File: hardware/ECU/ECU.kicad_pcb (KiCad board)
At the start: 4 copper layers, 58 x 69 mm, 75 parts, among them IC1 IR4427SPBF, IC2 EL357NB_TA_-G, IC3 EL357NB_TA_-G, J1 USB_B_Micro, J2 TFP09-2-12B, J3 Connector, Q1 S8050, Q2 S8050, Q3 RJP63K2, Q4 RJP63K2, SW1 RESET, SW2 EN, U1 AMS1117-3.3, U2 AMS1117-3.3, U3 CP2102N-Axx-xQFN28, U4 ESP32-WROOM-32U

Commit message: ECU hardware v0.2 candidate
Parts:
- removed C15: 22u, Capacitor_SMD:C_0603_1608Metric_Pad1.08x0.95mm_HandSolder
- removed C22, C23: 1n, Capacitor_SMD:C_0603_1608Metric_Pad1.08x0.95mm_HandSolder
- removed D11: LED, LED_SMD:LED_0603_1608Metric_Pad1.05x0.95mm_HandSolder
- removed Q2: S8050, Package_TO_SOT_SMD:SOT-23
- removed U3: CP2102N-Axx-xQFN28, Package_DFN_QFN:QFN-28-1EP_5x5mm_P0.5mm_EP3.35x3.35mm
- added C24: 100n, Capacitor_SMD:C_0603_1608Metric, F.Cu at (154.6, 133.4)
- added C25: 100n, Capacitor_SMD:C_0603_1608Metric, F.Cu at (149.2, 130.9)
- added C26: 100n, Capacitor_SMD:C_0603_1608Metric, F.Cu at (150.0, 114.3)
- added C27: 100n, Capacitor_SMD:C_0603_1608Metric, F.Cu at (146.1, 79.4)
- added C28: 100n, Capacitor_SMD:C_0603_1608Metric, F.Cu at (150.6, 79.4)
- added C29: 100n, Capacitor_SMD:C_0603_1608Metric, F.Cu at (152.9, 83.0)
- added IC4: ESP32-S3-WROOM-1U-N8R8, MyLibrary:ESP32S3WROOM1UN4, F.Cu at (130.1, 111.0)
- added IC5: EL357NB_TA_-G, MyLibrary:EL357NG, F.Cu at (150.8, 109.3)
- added J4: USB_B, Connector_USB:USB_B_TE_5787834_Vertical, F.Cu at (128.4, 87.9)
- added J5: BATTERY, Connector_Molex:Molex_KK-396_5273-02A_1x02_P3.96mm_Vertical, F.Cu at (165.4, 124.2)
- added J6: GATEs, Connector_Molex:Molex_KK-396_5273-06A_1x06_P3.96mm_Vertical, F.Cu at (209.7, 83.3)
- added J8: CAPTURE_TRG, Connector_JST:JST_XH_B2B-XH-A_1x02_P2.50mm_Vertical, F.Cu at (149.2, 118.2)
- added JP1: BOOT, Connector_PinHeader_2.54mm:PinHeader_1x02_P2.54mm_Vertical, F.Cu at (117.0, 118.0)
- added L1: 100u, MyLibrary:INDPM102100X400N, F.Cu at (187.2, 121.3)
- added R26: 10k, Resistor_SMD:R_0603_1608Metric_Pad0.98x0.95mm_HandSolder, F.Cu at (146.1, 86.3)
- added R27: 100, Resistor_SMD:R_0603_1608Metric_Pad0.98x0.95mm_HandSolder, F.Cu at (135.0, 95.9)
- added R28: 100, Resistor_SMD:R_0603_1608Metric_Pad0.98x0.95mm_HandSolder, F.Cu at (136.9, 85.0)
- added R30: 1k, Resistor_SMD:R_0603_1608Metric_Pad0.98x0.95mm_HandSolder, F.Cu at (134.1, 84.1)
- added R31: 1k, Resistor_SMD:R_0603_1608Metric_Pad0.98x0.95mm_HandSolder, F.Cu at (142.5, 121.2)
- added R32: 10k, Resistor_SMD:R_0603_1608Metric_Pad0.98x0.95mm_HandSolder, F.Cu at (149.1, 86.3)
- added R33: 100, Resistor_SMD:R_0603_1608Metric_Pad0.98x0.95mm_HandSolder, F.Cu at (143.8, 79.8)
- added R34: 100, Resistor_SMD:R_0603_1608Metric_Pad0.98x0.95mm_HandSolder, F.Cu at (152.9, 79.8)
- added R35: 10k, Resistor_SMD:R_0603_1608Metric_Pad0.98x0.95mm_HandSolder, F.Cu at (150.6, 86.3)
- added R36: 100, Resistor_SMD:R_0603_1608Metric_Pad0.98x0.95mm_HandSolder, F.Cu at (149.1, 78.6)
- added R37: 100, Resistor_SMD:R_0603_1608Metric_Pad0.98x0.95mm_HandSolder, F.Cu at (147.6, 78.6)
- added R38: 0, Resistor_SMD:R_0603_1608Metric_Pad0.98x0.95mm_HandSolder, F.Cu at (176.9, 106.8)
- added R39: 100, Resistor_SMD:R_0603_1608Metric_Pad0.98x0.95mm_HandSolder, F.Cu at (156.3, 133.5)
- added R42: 10k, Resistor_SMD:R_0603_1608Metric_Pad0.98x0.95mm_HandSolder, F.Cu at (152.6, 136.3)
- added R43: 10k, Resistor_SMD:R_0603_1608Metric_Pad0.98x0.95mm_HandSolder, F.Cu at (149.1, 136.3)
- added R45: 0.01, MyLibrary:RESC10052X106N, F.Cu at (165.4, 133.6)
- added R47: 130k, Resistor_SMD:R_0603_1608Metric_Pad0.98x0.95mm_HandSolder, F.Cu at (152.4, 129.4)
- added R50: 5.6k, Resistor_SMD:R_0603_1608Metric_Pad0.98x0.95mm_HandSolder, F.Cu at (152.4, 130.9)
- added R51: 10k, Resistor_SMD:R_0603_1608Metric_Pad0.98x0.95mm_HandSolder, F.Cu at (144.7, 133.7)
- added R52: 1k, Resistor_SMD:R_0603_1608Metric_Pad0.98x0.95mm_HandSolder, F.Cu at (146.7, 114.3)
- added R53: 1k, Resistor_SMD:R_0603_1608Metric_Pad0.98x0.95mm_HandSolder, F.Cu at (141.5, 113.7)
- added R54: 1k, Resistor_SMD:R_0603_1608Metric_Pad0.98x0.95mm_HandSolder, F.Cu at (137.5, 71.8)
- added U5: ADS1115IDGS, Package_SO:TSSOP-10_3x3mm_P0.5mm, F.Cu at (149.5, 133.6)
- added U6: INA180A3, Package_TO_SOT_SMD:SOT-23-5, F.Cu at (159.5, 133.6)
- added U7: SRV05-4, Package_TO_SOT_SMD:SOT-23-6, F.Cu at (122.6, 97.5)
- C10, C12: value 10u -> 100n; footprint Capacitor_SMD:C_0603_1608Metric_Pad1.08x0.95mm_HandSolder -> Capacitor_SMD:C_0603_1608Metric
- C11: footprint Capacitor_SMD:C_0603_1608Metric_Pad1.08x0.95mm_HandSolder -> Capacitor_SMD:C_0603_1608Metric
- C13: value 1n -> 100n; footprint Capacitor_SMD:C_0603_1608Metric_Pad1.08x0.95mm_HandSolder -> Capacitor_SMD:C_0603_1608Metric
- C14: footprint Capacitor_SMD:C_0603_1608Metric_Pad1.08x0.95mm_HandSolder -> Capacitor_SMD:C_0603_1608Metric; moved to F.Cu
- C16, D1, R2: moved to F.Cu
- C21: value 1n -> 100n; footprint Capacitor_SMD:C_0603_1608Metric_Pad1.08x0.95mm_HandSolder -> Capacitor_SMD:C_0603_1608Metric; moved to B.Cu
- C3, C4: footprint Capacitor_SMD:C_0805_2012Metric_Pad1.18x1.45mm_HandSolder -> Capacitor_SMD:C_0603_1608Metric
- C5: value 100n -> 1u; footprint Capacitor_SMD:C_0805_2012Metric_Pad1.18x1.45mm_HandSolder -> Capacitor_SMD:C_0603_1608Metric
- C8: value 22u -> 100u; footprint Capacitor_SMD:C_0805_2012Metric_Pad1.18x1.45mm_HandSolder -> Capacitor_SMD:CP_Elec_10x10
- C9: value 100n -> 1n; footprint Capacitor_SMD:C_0603_1608Metric_Pad1.08x0.95mm_HandSolder -> Capacitor_SMD:CP_Elec_10x10
- D10: value 1n4007 -> m7
- D3: value LED -> ss36; footprint LED_SMD:LED_0603_1608Metric_Pad1.05x0.95mm_HandSolder -> Diode_SMD:D_SMC; moved to F.Cu
- D4: value 3.6v -> 5v
- D5: value 1n4001 -> LED; footprint Diode_SMD:D_SMA -> LED_SMD:LED_0603_1608Metric_Pad1.05x0.95mm_HandSolder
- D6: value 5v -> ss36; footprint Diode_SMD:D_SOD-523 -> Diode_SMD:D_SMC
- D7: value 5v -> m7; footprint Diode_SMD:D_SOD-523 -> Diode_SMD:D_SMA
- D8: value LED -> ss36; footprint LED_SMD:LED_0603_1608Metric_Pad1.05x0.95mm_HandSolder -> Diode_SMD:D_SMC
- IC1: footprint My_Lirbrary:SOIC127P600X175-8N -> MyLibrary:SOIC127P600X175-8N
- IC2, IC3: footprint My_Lirbrary:SOP254P700X200-4N -> MyLibrary:EL357NG
- J1: value USB_B_Micro -> AQS; footprint Connector_USB:USB_Micro-B_Molex-105017-0001 -> Connector_JST:JST_XH_B6B-XH-A_1x06_P2.50mm_Vertical
- J2: footprint My_Lirbrary:TFP09212B -> MyLibrary:TFP09212B
- J3: value Connector -> CAM_SENSOR; footprint Connector_PinHeader_2.54mm:PinHeader_2x06_P2.54mm_Vertical -> Connector_JST:JST_XH_B6B-XH-A_1x06_P2.50mm_Vertical
- Q1: value S8050 -> RJP63K2; footprint Package_TO_SOT_SMD:SOT-23 -> Package_TO_SOT_SMD:TO-263-2; moved to F.Cu
- R1: value 1M -> 10k; moved to F.Cu
- R16, R17, R18, R19, R20, R21: footprint Resistor_SMD:R_0603_1608Metric_Pad0.98x0.95mm_HandSolder -> Resistor_SMD:R_0603_1608Metric; moved to F.Cu
- R22, R23: value 470 -> 10k
- R24: value 5k -> 10k
- R25: value 1k -> 10k
- R3: value 2k -> 10k; moved to F.Cu
- R4, R5, R8: value 12k -> 10k; moved to F.Cu
- R6, R7: value 0 -> 10k
- R9: value 2k -> 100
- SW1: value RESET -> RESET BTN; footprint Button_Switch_SMD:SW_Push_1P1T_NO_CK_KMR2 -> Button_Switch_SMD:SW_SPST_PTS810
- SW2: value EN -> ZERO BTN; footprint Button_Switch_SMD:SW_Push_1P1T_NO_CK_KMR2 -> Button_Switch_SMD:SW_SPST_PTS810
- U1: value AMS1117-3.3 -> LM2576S-5; footprint Package_TO_SOT_SMD:SOT-223-3_TabPin2 -> Package_TO_SOT_SMD:TO-263-5_TabPin3
- U4: value ESP32-WROOM-32U -> ADS1115IDGS; footprint RF_Module:ESP32-WROOM-32U -> Package_SO:TSSOP-10_3x3mm_P0.5mm
- moved D10 81.3 mm to (159.7, 143.2), turned to 0 degrees
- moved C8 77.2 mm to (209.8, 134.6), turned to -90 degrees
- moved C2 70.4 mm to (118.0, 141.2), turned to 180 degrees
- moved C7 70.4 mm to (118.0, 139.1), turned to 180 degrees
- moved D3 67.6 mm to (201.3, 124.2), turned to 0 degrees
- moved C6 67.4 mm to (119.0, 127.3)
- moved C1 67.4 mm to (119.0, 125.2)
- moved U2 66.1 mm to (118.0, 133.1), turned to 90 degrees
- moved U1 64.3 mm to (196.2, 138.3)
- moved R22 62.5 mm to (119.8, 98.6), turned to 90 degrees
- moved R5 61.0 mm to (143.8, 136.1), turned to 90 degrees
- moved R24 60.8 mm to (144.7, 132.1), turned to 180 degrees
- moved R4 59.5 mm to (145.3, 137.0), turned to 90 degrees
- moved R8 59.0 mm to (113.2, 111.9)
- moved Q4 57.6 mm to (188.6, 93.2), turned to 0 degrees
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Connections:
- net Net-(J2-CD/DAT3) renamed /SD_DAT3
- net Net-(J2-DAT2) renamed /SD_DAT2
- C10 pad 1: VBUS -> GND
- C10 pad 2: GND -> +3.3V
- C11 pad 1: +3.3V -> GND
- C11 pad 2: GND -> Net-(C11-Pad2)
- C12 pad 1: +3.3V -> GND
- C12 pad 2: GND -> Net-(C12-Pad2)
- C13 pad 1: /EN -> GND
- C13 pad 2: GND -> +3.3V
- C14 pad 2: +3.3V -> Net-(U4-AIN3)
- C18 pad 1: +12V -> +BATT
- C19 pad 1: +12V -> +BATT
- C2 pad 1: +12V -> +4V
- C21 pad 2: /O2 -> +3.3V
- C3 pad 1: VBUS -> GND
- C3 pad 2: GND -> +3.3V
- C4 pad 1: VBUS -> GND
- C4 pad 2: GND -> +3.3V
- C5 pad 1: +3.3V -> GND
- C5 pad 2: GND -> /RESET_PIN
- C7 pad 1: +12V -> +4V
- C8 pad 1: +3.3V -> +BATT
- C9 pad 1: VBUS -> +5V
- D10 pad 1: +12V -> +4V
- D10 pad 2: +BATT -> +5V
- D3 pad 1: GND -> Net-(D3-K)
- D3 pad 2: Net-(D3-A) -> GND
- D4 pad 1: +3.3V -> +4V
- D5 pad 1: VBUS -> Net-(D5-K)
- D5 pad 2: Net-(D5-A) -> /LED_PIN
- D6 pad 1: Net-(D6-K) -> +BATT
- D6 pad 2: GND -> /FUEL
- D7 pad 1: Net-(D7-K) -> +4V
- D7 pad 2: GND -> Net-(D7-A)
- D8 pad 1: GND -> +BATT
- D8 pad 2: Net-(D8-A) -> /PUMP
- IC1 pad 5: /COIL_IGBT -> Net-(IC1-OUT_B)
- IC1 pad 6: +12V -> +BATT
- IC1 pad 7: /FUEL_IGBT -> Net-(IC1-OUT_A)
- IC2 pad 1: /FUEL_PIN -> /COIL_PIN
- IC2 pad 4: +12V -> +BATT
- IC3 pad 1: /COIL_PIN -> /FUEL_PIN
- IC3 pad 4: +12V -> +BATT
- J1 pad 1: Net-(D5-A) -> GND
- J1 pad 2: Net-(D6-K) -> /IAT
- J1 pad 3: Net-(D7-K) -> /MPS
- J1 pad 4: unconnected-(J1-ID-Pad4) -> /TPS
- J1 pad 5: GND -> /AFR
- J1 pad 6: Net-(J1-Shield) -> +5V
- J2 pad 8: Net-(J2-DAT1) -> /SD_DAT1
- J3 pad 1: +BATT -> GND
- J3 pad 2: /FUEL -> /FSPI_CS
- J3 pad 3: GND -> /FSPI_MOSI
- J3 pad 4: /COIL -> /FSPI_CLK
- J3 pad 5: GND -> /FSPI_MISO
- J3 pad 6: GND -> +5V
- Q1 pad 1: Net-(Q1-E) -> Net-(Q1-G)
- Q1 pad 2: Net-(Q1-B) -> /PUMP
- Q1 pad 3: /EN -> GND
- R1 pad 1: Net-(J1-Shield) -> GND
- R1 pad 2: GND -> Net-(IC1-INA)
- R11 pad 2: /COIL_IGBT -> Net-(IC1-OUT_A)
- R15 pad 2: /FUEL_IGBT -> Net-(IC1-OUT_B)
- R2 pad 1: +12V -> +4V
- R21 pad 1: Net-(J2-DAT1) -> +3.3V
- R21 pad 2: +3.3V -> /SD_DAT1
- R22 pad 1: Net-(C22-Pad1) -> Net-(IC4-IO46)
- R22 pad 2: /IO0 -> GND
- R23 pad 1: Net-(C23-Pad1) -> GND
- R23 pad 2: /EN -> Net-(IC5-E)
- R24 pad 1: /IO0 -> Net-(U5-AIN2)
- R25 pad 1: GND -> /SDA_0
- R25 pad 2: Net-(D11-K) -> +3.3V
- R3 pad 1: VBUS -> GND
- R3 pad 2: Net-(D3-A) -> Net-(IC1-INB)
- R4 pad 1: Net-(Q2-E) -> +3.3V
- R4 pad 2: Net-(Q1-B) -> /SCL_1
- R5 pad 1: Net-(Q1-E) -> +3.3V
- R5 pad 2: Net-(Q2-B) -> /SDA_1
- R6 pad 1: Net-(U3-RXD) -> /RESET_PIN
- R6 pad 2: /RXD -> +3.3V
- R7 pad 2: /TXD -> +3.3V
- R8 pad 1: /EN -> GND
- R8 pad 2: +3.3V -> Net-(IC4-IO45)
- R9 pad 1: +3.3V -> GND
- R9 pad 2: Net-(D8-A) -> Net-(IC5-K)
- SW1 pad 2: Net-(C22-Pad1) -> Net-(C11-Pad2)
- SW2 pad 2: Net-(C23-Pad1) -> Net-(C12-Pad2)
- U1 pad 1: GND -> +BATT
- U1 pad 2: +3.3V -> Net-(D3-K)
- U1 pad 3: VBUS -> GND
- U2 pad 3: +12V -> +4V
- U4 pad 1: GND -> Net-(U4-ADDR)
- U4 pad 10: unconnected-(U4-IO25-Pad10) -> /SCL_0
- U4 pad 2: +3.3V -> Net-(U4-ALERT/RDY)
- U4 pad 3: /EN -> GND
- U4 pad 4: unconnected-(U4-SENSOR_VP-Pad4) -> Net-(U4-AIN0)
- U4 pad 5: unconnected-(U4-SENSOR_VN-Pad5) -> Net-(U4-AIN1)
- U4 pad 7: unconnected-(U4-IO35-Pad7) -> Net-(U4-AIN3)
- U4 pad 8: unconnected-(U4-IO32-Pad8) -> +3.3V
- U4 pad 9: unconnected-(U4-IO33-Pad9) -> /SDA_0
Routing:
- net +BATT: track 4.48 -> 257.3 mm, vias 0 -> 8
- net +5V: track 0.00 -> 195.7 mm, vias 0 -> 3
- net GND: track 3.96 -> 105.0 mm, vias 157 -> 195
- net +4V: track 0.00 -> 72.6 mm
- net Net-(D7-A): track 0.00 -> 48.3 mm, vias 0 -> 4
- net /FSPI_MISO: track 0.00 -> 46.3 mm
- net /FSPI_CLK: track 0.00 -> 44.2 mm
- net /FSPI_MOSI: track 0.00 -> 42.2 mm
- net /FSPI_CS: track 0.00 -> 40.1 mm
- net +12V: track 38.6 -> 0.00 mm, vias 6 -> 0
- net VBUS: track 38.3 -> 0.00 mm, vias 2 -> 0
- net /VSPI_MOSI: track 35.8 -> 0.00 mm, vias 1 -> 0
- net Net-(Q1-E): track 35.1 -> 0.00 mm, vias 1 -> 0
- net /SDA_0: track 0.00 -> 33.9 mm
- net /SCL_0: track 0.00 -> 32.2 mm
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- removed copper zone on In2.Cu, net +12V
- removed copper zone on In1.Cu, net GND
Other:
- board size 58 x 69 mm -> 115 x 100 mm
- copper layers 4 -> 2
- board text added: "+"
- board text added: "+5v"
- board text added: "-"
- board text added: "AFR"
- board text added: "BOOT"
- board text added: "CAMSHAFT SENSOR"
- board text added: "CPTR"
- board text added: "ECU v0.2 Author: Collyn"
- board text added: "FUEL CONTROL SENSOR"
- board text added: "IAT"
- board text added: "MPS"
- board text added: "PWR"
- board text added: "RST"
- board text added: "TPS"
- board text added: "ZERO"
- board text removed: "COIL"
- board text removed: "ECU v0.1 Author: Collyn"
- board text removed: "EN"
- board text removed: "FUEL"
- board text removed: "O2"
- board text removed: "RESET"

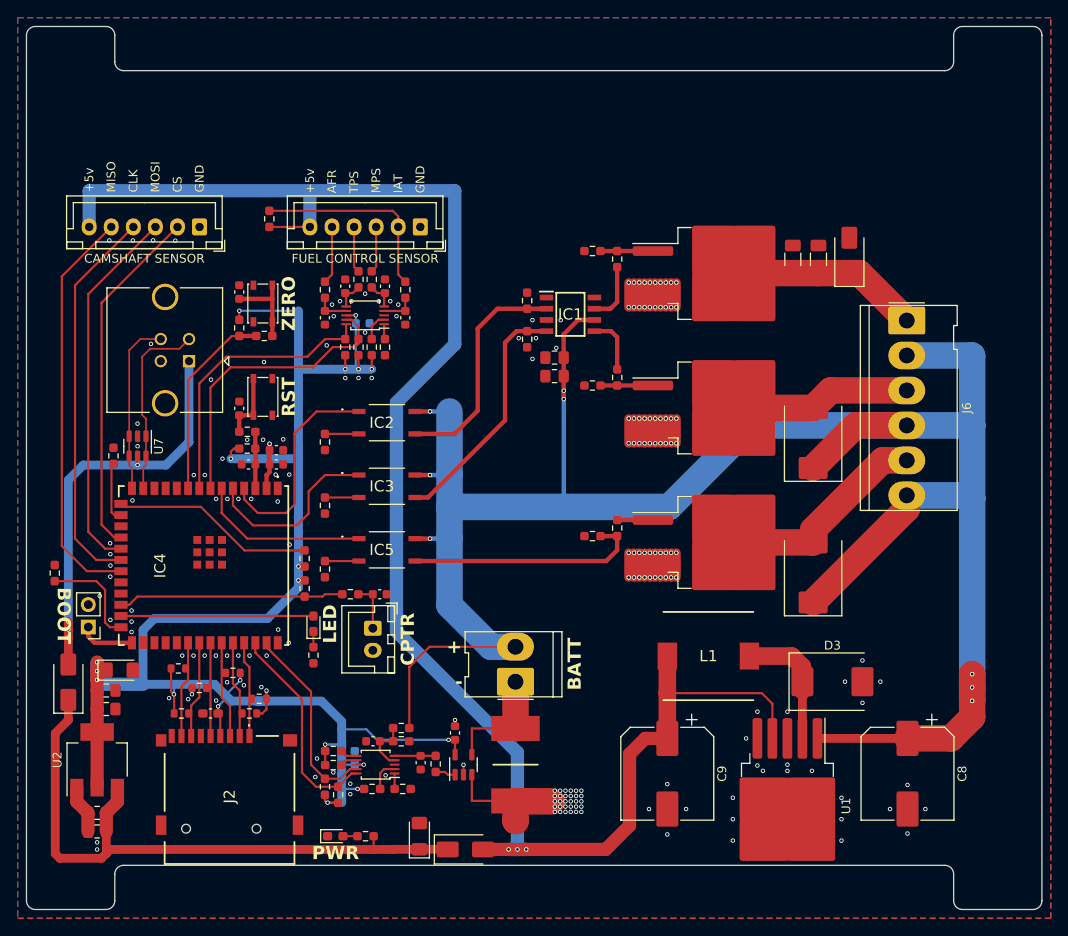
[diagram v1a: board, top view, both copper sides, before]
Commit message: add idle control circuit
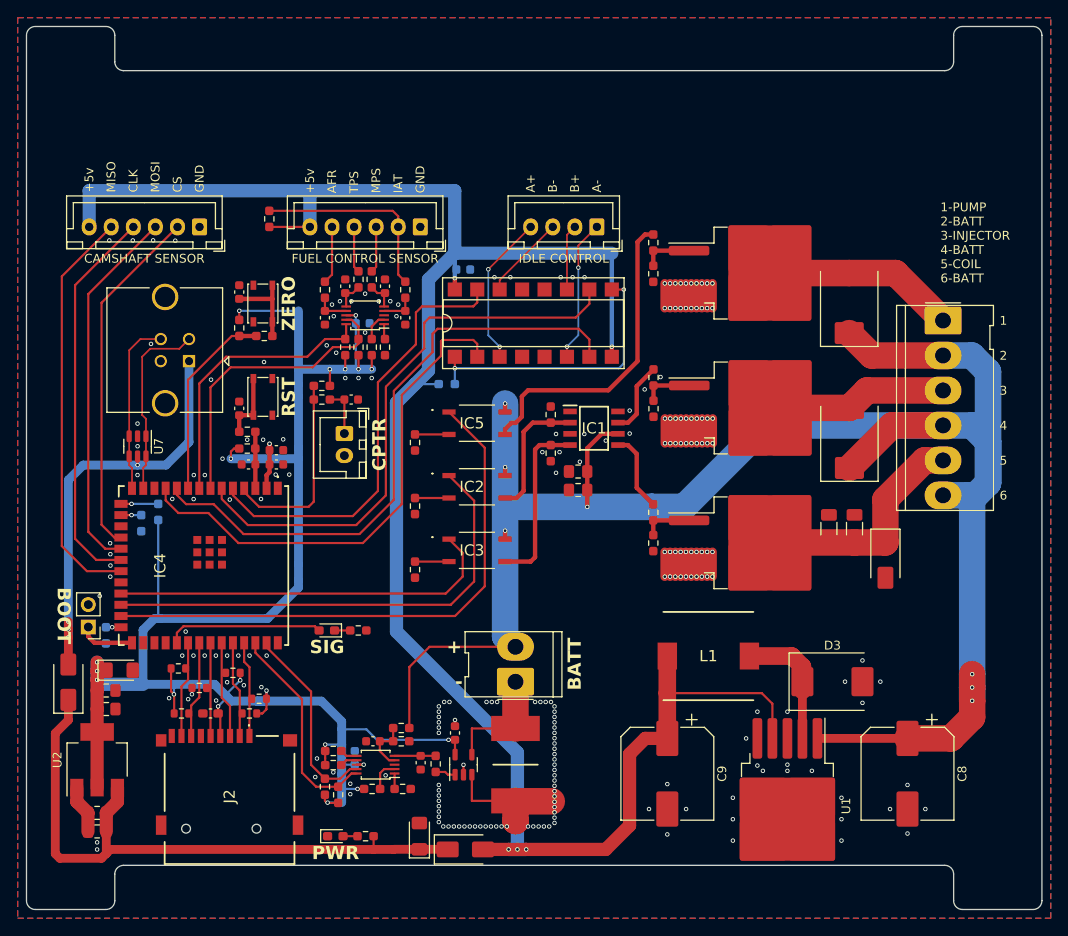
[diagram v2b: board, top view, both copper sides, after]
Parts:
- added C15: 100n, Capacitor_SMD:C_0603_1608Metric, B.Cu at (159.5, 77.5)
- added J7: ISC Control, Connector_JST:JST_XH_B4B-XH-A_1x04_P2.50mm_Vertical, F.Cu at (174.6, 72.7)
- added R29: 10k, Resistor_SMD:R_0603_1608Metric_Pad0.98x0.95mm_HandSolder, B.Cu at (157.6, 90.5)
- added U3: L293D, Package_DIP:DIP-16_W7.62mm_SMDSocket_SmallPads, F.Cu at (167.4, 83.6)
- R22, R7, R8: moved to B.Cu
- moved D9 34.7 mm to (207.3, 110.4), turned to -90 degrees
- moved R10 33.8 mm to (181.0, 108.5), turned to -90 degrees
- moved R38 32.6 mm to (181.0, 74.5), turned to 90 degrees
- moved Q1 30.8 mm to (192.7, 77.9)
- moved C17 30.8 mm to (200.9, 106.9)
- moved C20 30.8 mm to (203.8, 106.9)
- moved D8 30.8 mm to (203.2, 81.3)
- moved Q3 30.8 mm to (192.7, 108.5)
- moved R23 30.5 mm to (181.0, 78.0), turned to 90 degrees
- moved R11 29.0 mm to (181.0, 105.0), turned to 90 degrees
- moved R53 23.0 mm to (143.4, 90.7), turned to 0 degrees
- moved J8 22.3 mm to (146.0, 96.1)
- moved R52 22.3 mm to (143.4, 92.2)
- moved C26 22.3 mm to (146.8, 92.2)
- moved IC5 17.6 mm to (161.0, 94.9)
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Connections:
- IC2 pad 1: /COIL_PIN -> /FUEL_PIN
- IC3 pad 1: /FUEL_PIN -> /COIL_PIN
- IC4 pad 10: unconnected-(IC4-IO17-Pad10) -> /ISC_AN_PIN
- IC4 pad 11: unconnected-(IC4-IO18-Pad11) -> /ISC_AP_PIN
- IC4 pad 23: unconnected-(IC4-IO21-Pad23) -> /COIL_PIN
- IC4 pad 24: /CAPTURE_PIN -> /FUEL_PIN
- IC4 pad 25: /LED_PIN -> /FUEL_PUMP_PIN
- IC4 pad 31: unconnected-(IC4-IO38-Pad31) -> /LED_PIN
- IC4 pad 4: /COIL_PIN -> /CAPTURE_PIN
- IC4 pad 5: /FUEL_PIN -> /ISC_BN_PIN
- IC4 pad 6: /FUEL_PUMP_PIN -> /ISC_BP_PIN
- J6 pad 1: /COIL -> /PUMP
- J6 pad 5: /PUMP -> /COIL
- R11 pad 2: Net-(IC1-OUT_A) -> Net-(IC1-OUT_B)
- R15 pad 2: Net-(IC1-OUT_B) -> Net-(IC1-OUT_A)
- R23 pad 2: Net-(IC5-E) -> Net-(Q1-G)
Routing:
- net /ISC_AN_PIN: track 0.00 -> 69.8 mm
- net /ISC_BP_PIN: track 0.00 -> 64.9 mm
- net /ISC_AP_PIN: track 0.00 -> 58.0 mm
- net /ISC_BN_PIN: track 0.00 -> 50.2 mm
- net /FUEL_PUMP_PIN: track 19.6 -> 64.0 mm
- net +BATT: track 257.3 -> 220.6 mm, vias 8 -> 7
- net +5V: track 195.7 -> 232.0 mm, vias 3 -> 5
- net /FUEL_PIN: track 21.0 -> 54.3 mm
- net Net-(U3-EN1,2): track 0.00 -> 32.2 mm, vias 0 -> 2
- net /COIL_PIN: track 24.4 -> 44.4 mm
- net Net-(IC4-IO3): track 23.0 -> 4.22 mm, vias 0 -> 1
- net /ISC_AP: track 0.00 -> 17.2 mm, vias 0 -> 2
- net /ISC_AN: track 0.00 -> 16.1 mm, vias 0 -> 2
- net +3.3V: track 209.5 -> 221.2 mm, vias 22 -> 21
- net Net-(IC1-INA): track 26.2 -> 14.8 mm
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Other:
- board text added: "1"
- board text added: "1-PUMP 2-BATT 3-INJECTOR 4-BATT 5-COIL 6-BATT"
- board text added: "2"
- board text added: "3"
- board text added: "4"
- board text added: "5"
- board text added: "6"
- board text added: "A+"
- board text added: "A-"
- board text added: "B+"
- board text added: "B-"
- board text added: "IDLE CONTROL"
- board text added: "SIG"
- board text removed: "LED"
